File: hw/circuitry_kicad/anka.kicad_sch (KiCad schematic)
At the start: 41 parts, among them M1 Motor_Servo, U1 CC56-12EWA, U2 LM35-LP, U3 TSOP34S40F, U4 MAX7219

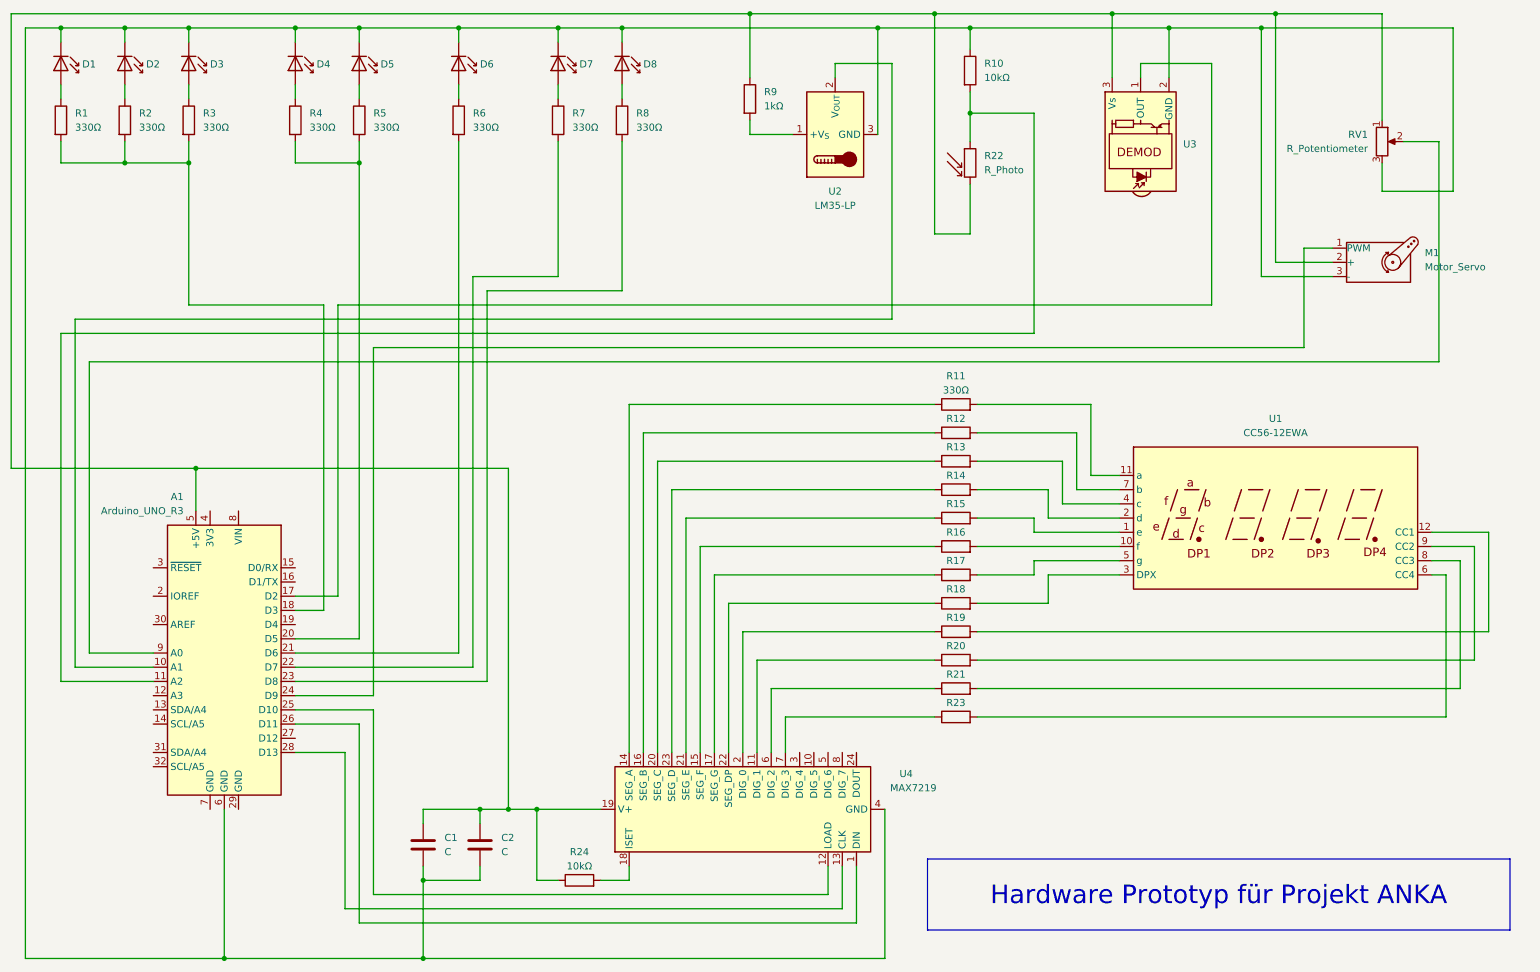
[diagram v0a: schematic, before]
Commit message: removed some errors from circuit diagram
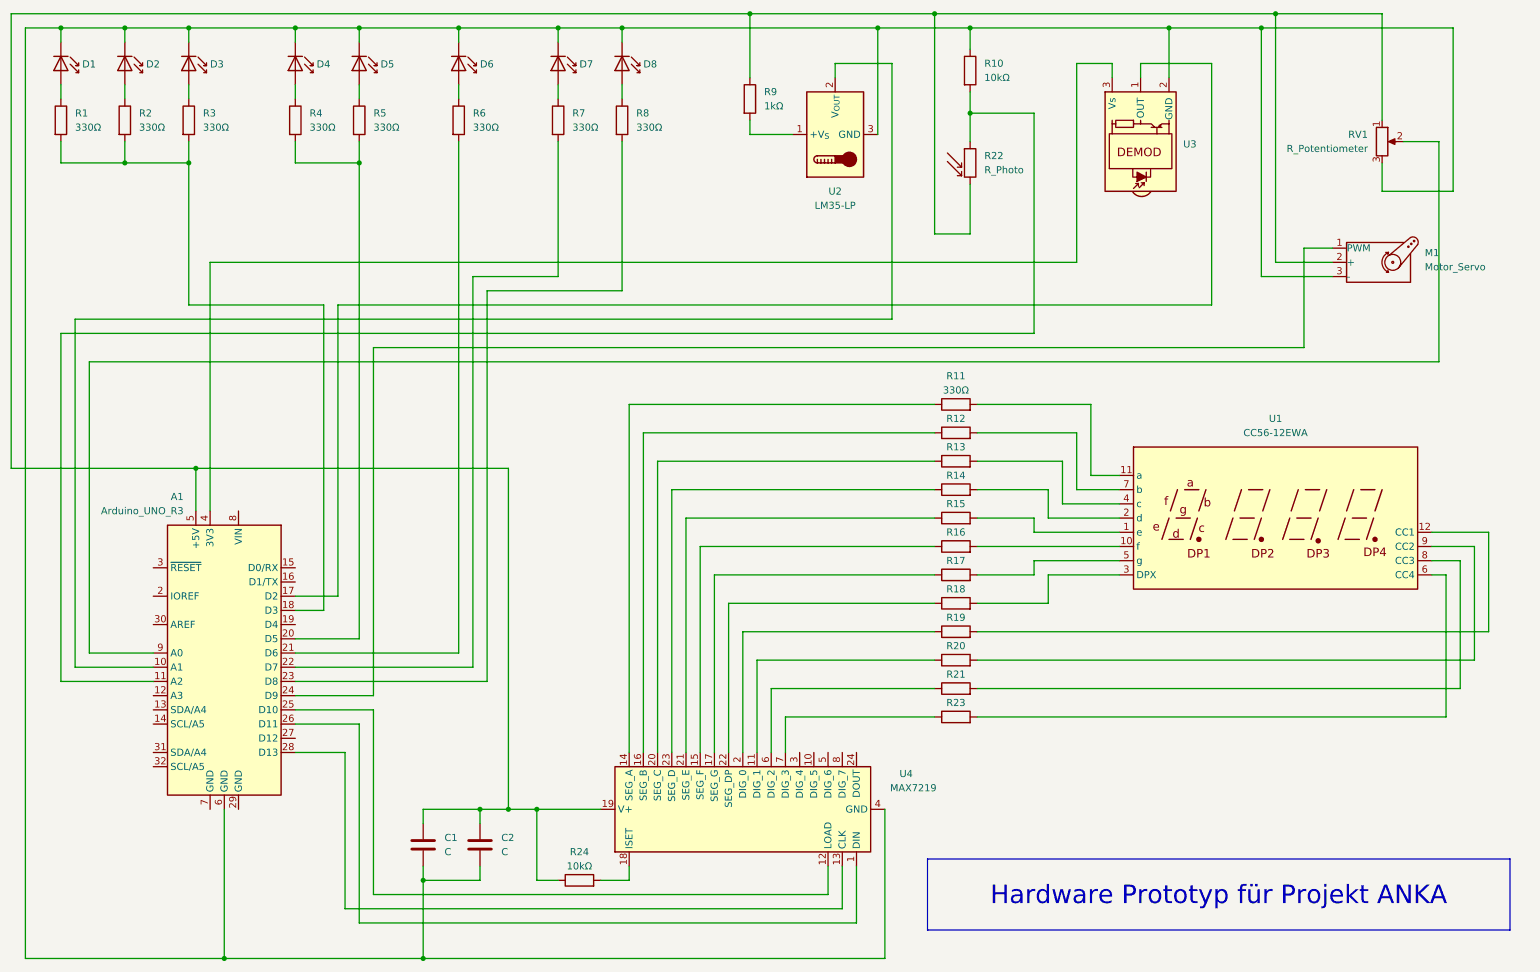
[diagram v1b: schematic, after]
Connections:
- net at A1.5 (+5V), C1.1, C2.1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: no longer U3.3 (Vs)
- net at A1.4 (3V3): now also U3.3 (Vs)
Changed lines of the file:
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@@
   (junction (at 109.22 158.75) (diameter 0) (color 0 0 0 0)
   )
-  (junction (at 212.09 16.51) (diameter 0) (color 0 0 0 0)
-  )
   (junction (at 180.34 16.51) (diameter 0) (color 0 0 0 0)
   )
@@
   (junction (at 222.25 19.05) (diameter 0) (color 0 0 0 0)
   )
-  (wire (pts (xy 212.09 16.51) (xy 212.09 27.94))
-    (stroke (width 0) (type default))
-  )
   (wire (pts (xy 147.32 16.51) (xy 147.32 27.94))
     (stroke (width 0) (type default))
@@
     (stroke (width 0) (type default))
   )
-  (wire (pts (xy 180.34 16.51) (xy 212.09 16.51))
+  (wire (pts (xy 180.34 16.51) (xy 241.3 16.51))
     (stroke (width 0) (type default))
   )
@@
     (stroke (width 0) (type default))
   )
+  (wire (pts (xy 212.09 25.4) (xy 212.09 27.94))
+    (stroke (width 0) (type default))
+  )
   (wire (pts (xy 95.25 19.05) (xy 113.03 19.05))
     (stroke (width 0) (type default))
@@
     (stroke (width 0) (type default))
   )
+  (wire (pts (xy 205.74 60.96) (xy 50.8 60.96))
+    (stroke (width 0) (type default))
+  )
   (wire (pts (xy 46.99 39.37) (xy 46.99 43.18))
     (stroke (width 0) (type default))
@@
     (stroke (width 0) (type default))
   )
+  (wire (pts (xy 50.8 60.96) (xy 50.8 105.41))
+    (stroke (width 0) (type default))
+  )
   (wire (pts (xy 251.46 63.5) (xy 238.76 63.5))
     (stroke (width 0) (type default))
@@
     (stroke (width 0) (type default))
   )
-  (wire (pts (xy 212.09 16.51) (xy 241.3 16.51))
-    (stroke (width 0) (type default))
-  )
   (wire (pts (xy 187.96 116.84) (xy 198.12 116.84))
     (stroke (width 0) (type default))
@@
     (stroke (width 0) (type default))
   )
+  (wire (pts (xy 212.09 25.4) (xy 205.74 25.4))
+    (stroke (width 0) (type default))
+  )
   (wire (pts (xy 187.96 111.76) (xy 213.36 111.76))
     (stroke (width 0) (type default))
@@
     (stroke (width 0) (type default))
   )
+  (wire (pts (xy 205.74 25.4) (xy 205.74 60.96))
+    (stroke (width 0) (type default))
+  )
